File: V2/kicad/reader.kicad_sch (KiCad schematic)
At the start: 88 parts, among them SW1 SW_Rezistance, SW2 SW_src, U1 STM32H523CET6, U2 MAX98357AETE+T, U3 MLD-TF PUSH-H18, U4 TCAN1057AVDRQ1, U5 ESD2CAN24-ES, U6 RJ-064-1, U7 MCP16301Hx-xCH, Y1 16MHz

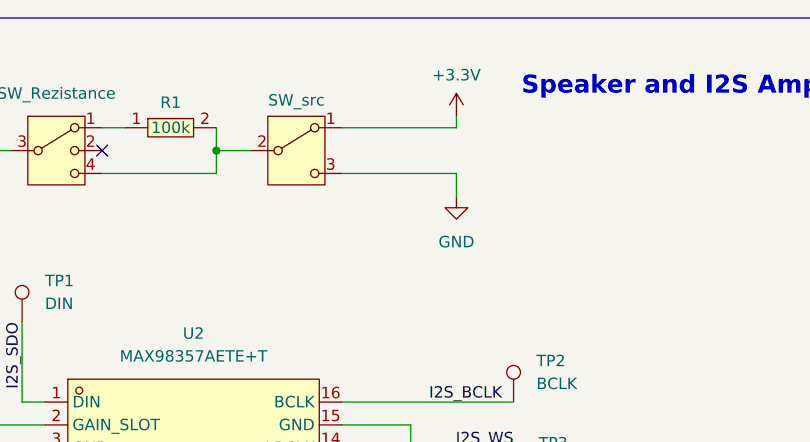
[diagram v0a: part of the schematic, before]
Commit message: changed signage in gain slot table
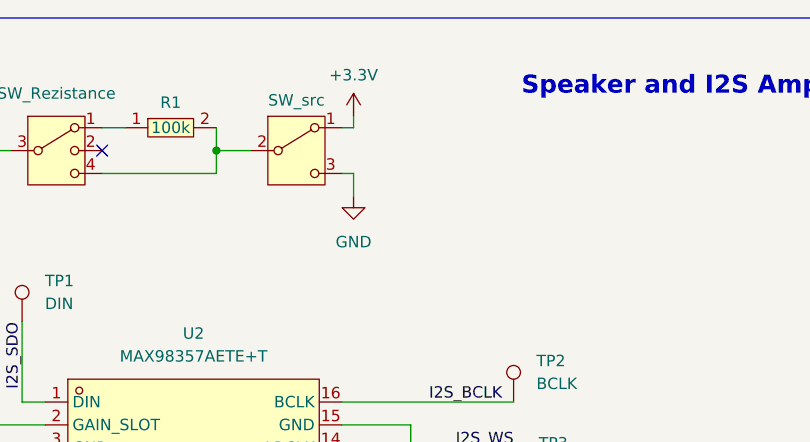
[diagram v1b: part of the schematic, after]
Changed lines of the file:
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@@
 	(wire
 		(pts
-			(xy 354.33 35.56) (xy 354.33 33.02)
+			(xy 342.9 35.56) (xy 342.9 33.02)
 		)
 		(stroke
@@
 	(wire
 		(pts
-			(xy 341.63 27.94) (xy 354.33 27.94)
+			(xy 341.63 27.94) (xy 342.9 27.94)
 		)
 		(stroke
@@
 	(wire
 		(pts
-			(xy 354.33 26.67) (xy 354.33 27.94)
+			(xy 342.9 26.67) (xy 342.9 27.94)
 		)
 		(stroke
@@
 	(wire
 		(pts
-			(xy 354.33 33.02) (xy 341.63 33.02)
+			(xy 342.9 33.02) (xy 341.63 33.02)
 		)
 		(stroke
@@
 				)
 			)
-			(table_cell "2"
+			(table_cell "1"
 				(exclude_from_sim no)
 				(at 285.242 22.352 0)
@@
 				)
 			)
-			(table_cell "3"
+			(table_cell "1"
 				(exclude_from_sim no)
 				(at 290.068 24.892 0)
@@
 				)
 			)
-			(table_cell "1"
+			(table_cell "2"
 				(exclude_from_sim no)
 				(at 285.242 27.432 0)
@@
 				)
 			)
-			(table_cell "2"
+			(table_cell "1"
 				(exclude_from_sim no)
 				(at 285.242 32.512 0)
@@
 				)
 			)
-			(table_cell "1"
+			(table_cell "3"
 				(exclude_from_sim no)
 				(at 290.068 32.512 0)
@@
 	(symbol
 		(lib_id "power:+3.3V")
-		(at 354.33 26.67 0)
+		(at 342.9 26.67 0)
 		(unit 1)
 		(body_style 1)
@@
 		(dnp no)
 		(property "Reference" "#PWR01"
-			(at 354.33 30.48 0)
+			(at 342.9 30.48 0)
 			(hide yes)
 			(show_name no)
@@
 		)
 		(property "Value" "+3.3V"
-			(at 354.33 22.098 0)
+			(at 342.9 22.098 0)
 			(show_name no)
 			(do_not_autoplace no)
@@
 		)
 		(property "Footprint" ""
-			(at 354.33 26.67 0)
+			(at 342.9 26.67 0)
 			(hide yes)
 			(show_name no)
@@
 		)
 		(property "Datasheet" ""
-			(at 354.33 26.67 0)
+			(at 342.9 26.67 0)
 			(hide yes)
 			(show_name no)
@@
 		)
 		(property "Description" "Power symbol creates a global label with name \"+3.3V\""
-			(at 354.33 26.67 0)
+			(at 342.9 26.67 0)
 			(hide yes)
 			(show_name no)
@@
 	(symbol
 		(lib_id "power:GND")
-		(at 354.33 35.56 0)
+		(at 342.9 35.56 0)
 		(unit 1)
 		(body_style 1)
@@
 		(fields_autoplaced yes)
 		(property "Reference" "#PWR02"
-			(at 354.33 41.91 0)
+			(at 342.9 41.91 0)
 			(hide yes)
 			(show_name no)
@@
 		)
 		(property "Value" "GND"
-			(at 354.33 40.64 0)
+			(at 342.9 40.64 0)
 			(show_name no)
 			(do_not_autoplace no)
@@
 		)
 		(property "Footprint" ""
-			(at 354.33 35.56 0)
+			(at 342.9 35.56 0)
 			(hide yes)
 			(show_name no)
@@
 		)
 		(property "Datasheet" ""
-			(at 354.33 35.56 0)
+			(at 342.9 35.56 0)
 			(hide yes)
 			(show_name no)
@@
 		)
 		(property "Description" "Power symbol creates a global label with name \"GND\" , ground"
-			(at 354.33 35.56 0)
+			(at 342.9 35.56 0)
 			(hide yes)
 			(show_name no)
@@
 			)
 		)
-		(property "Datasheet" "https://jlcpcb.com/api/file/downloadByFileSystemAccessId/8590908716709863424"
+		(property "Datasheet" "https://www.lcsc.com/datasheet/C6465979.pdf?spm=wm.sxq.inf.ggs&lcsc_vid=FVRbUlZVElUKAldUT1FbAVZWElcMUlFXR1FXBgVQElUxVlNeRlBeXl1SQlVfVzsOAxUeFF5JWBYZEEoKFBINSQcJGk4%3D"
 			(at 24.13 261.112 0)
 			(hide yes)
@@
 			)
 		)
-		(property "Datasheet" "https://jlcpcb.com/api/file/downloadByFileSystemAccessId/8590902847586181120"
+		(property "Datasheet" "https://www.lcsc.com/datasheet/C5553822.pdf"
 			(at 43.18 261.112 0)
 			(hide yes)

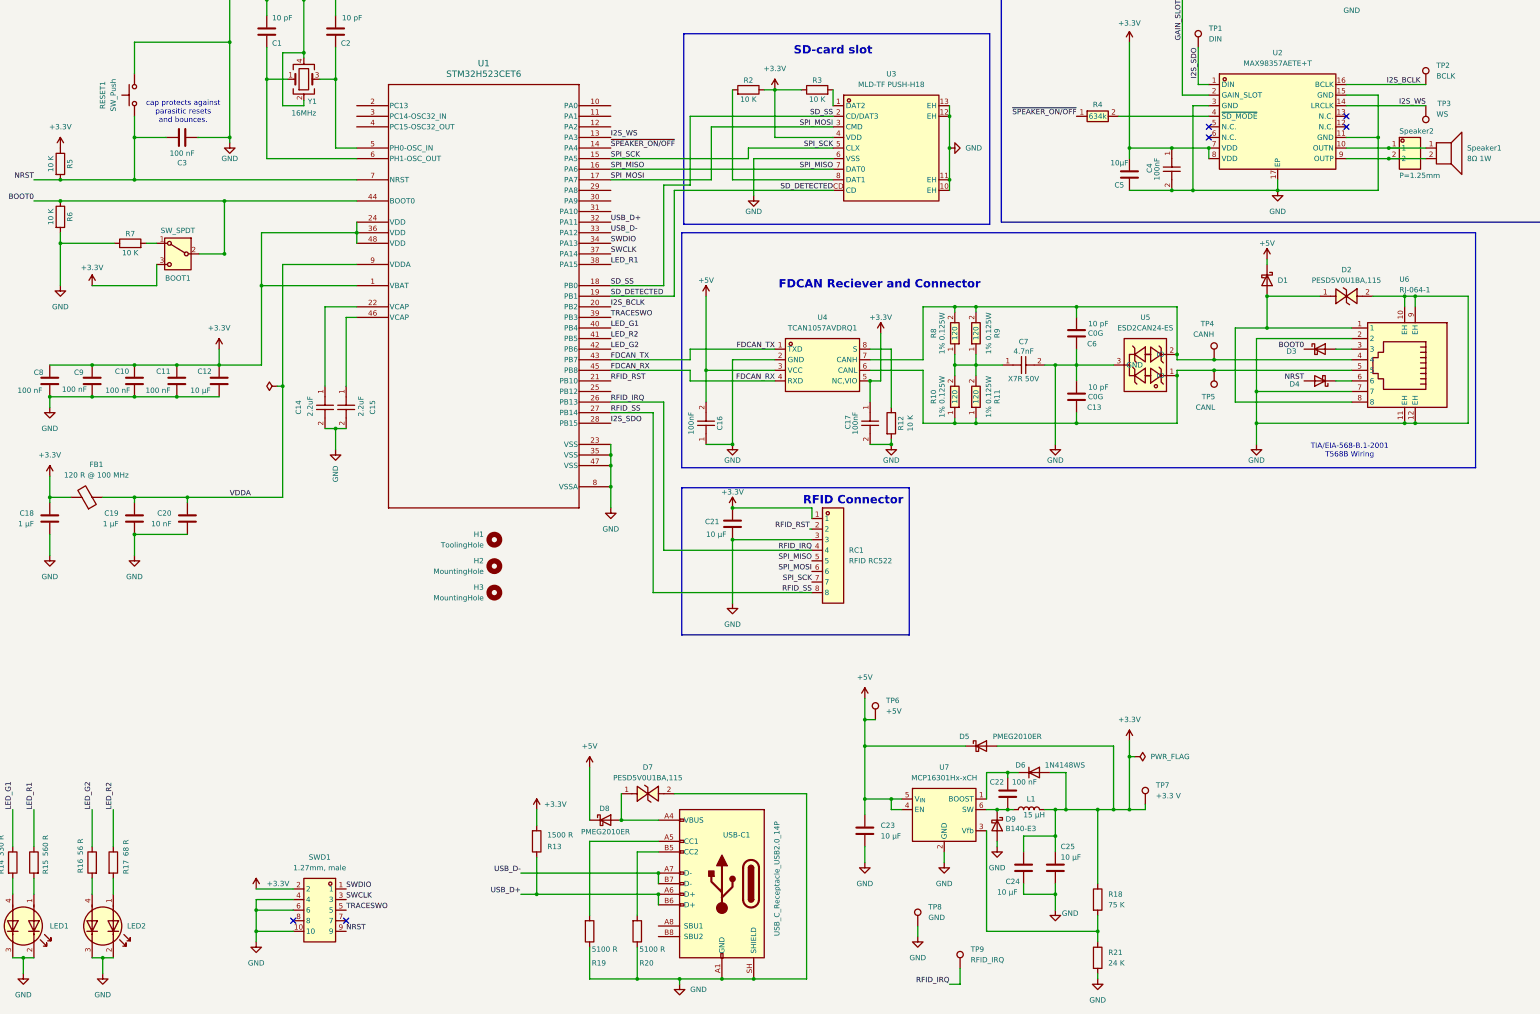
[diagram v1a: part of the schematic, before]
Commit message: changed 20mA led to 2mA led so both are same. changed orientation of card logo on back of board
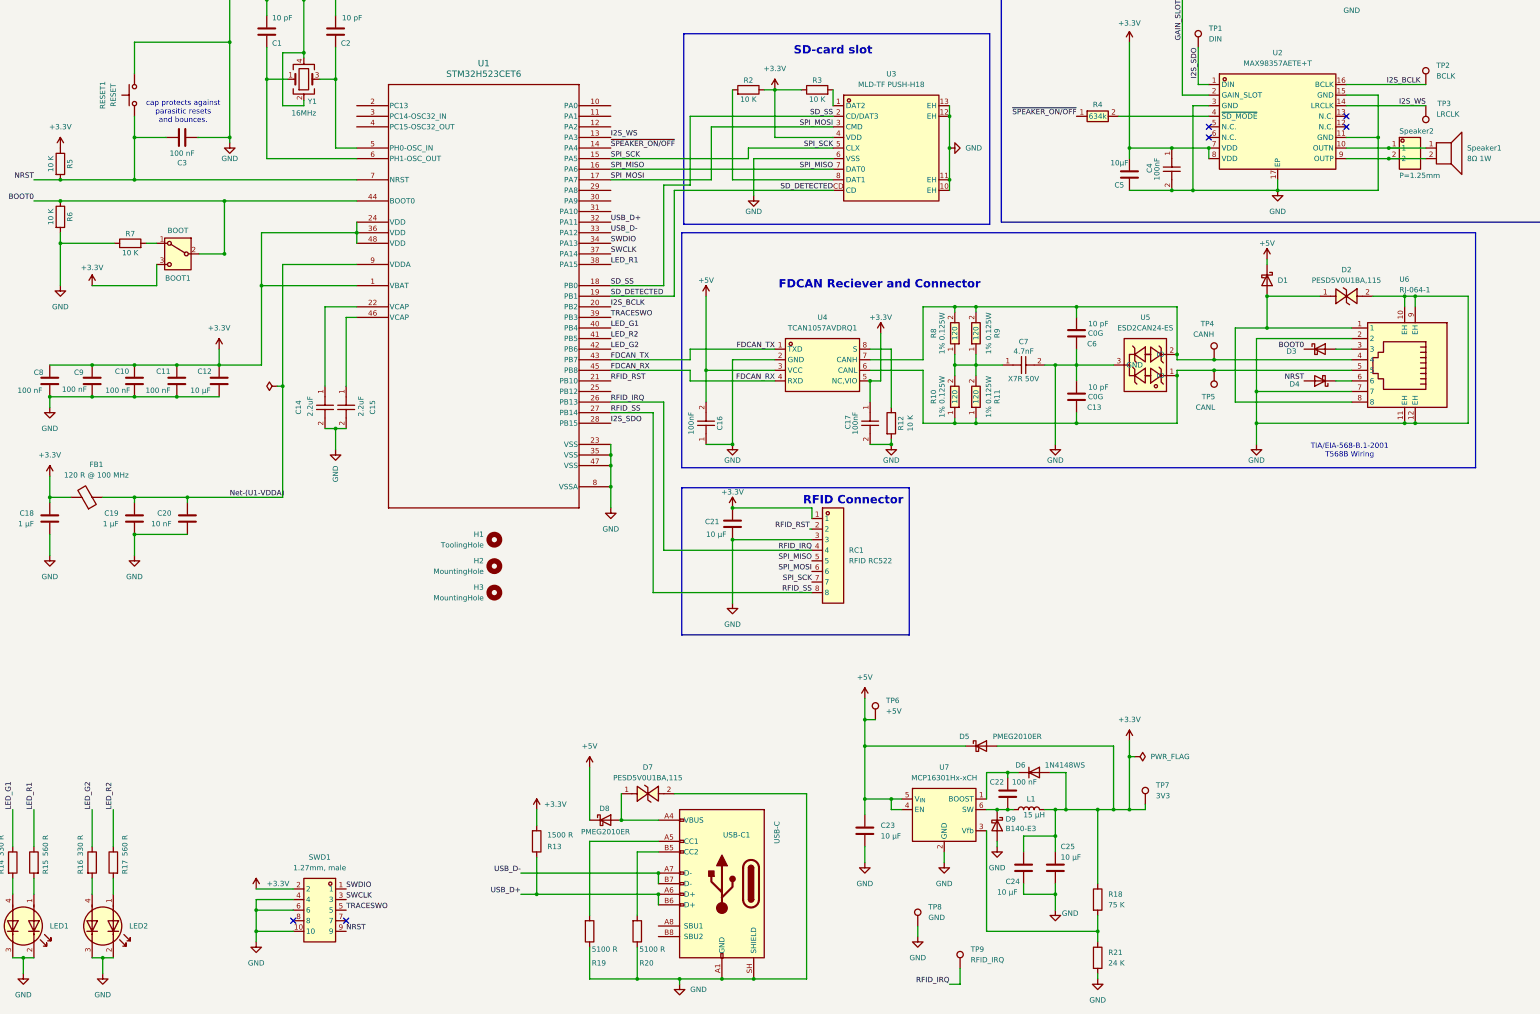
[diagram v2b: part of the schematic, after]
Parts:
- BOOT1: value SW_SPDT -> BOOT
- LED2: value APHBM2012SURKCGKC -> APHBM2012LSURKZGKC; JLCPCB https://jlcpcb.com/partdetail/Kingbright-APHBM2012SURKCGKC/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 -> https://jlcpcb.com/partdetail/Kingbright-APHBM2012LSURKZGKC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; LCSC C5553822 -> C6465979; Note 20mA, Red, Emerald, 120°, SMD-4P, 2 x 1.3 mm -> 2mA Red, Emerald, 120°, SMD-4P, 2 x 1.3 mm
- R16: value 56 R -> 330 R; JLCPCB https://jlcpcb.com/partdetail/25870-0402WGF560JTCE/C25127 -> https://jlcpcb.com/partdetail/25847-0402WGF3300TCE/C25104; LCSC C25127 -> C25104
- R17: value 68 R -> 560 R; JLCPCB https://jlcpcb.com/partdetail/Yageo-RC0402FR0768RL/C163455 -> https://jlcpcb.com/partdetail/C25126; LCSC C163455 -> C25126
- RESET1: value SW_Push -> RESET
- TP3: value WS -> LRCLK
- TP7: value +3.3 V -> 3V3
- USB-C1: value USB_C_Receptacle_USB2.0_14P -> USB-C
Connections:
- net VDDA renamed Net-(U1-VDDA)

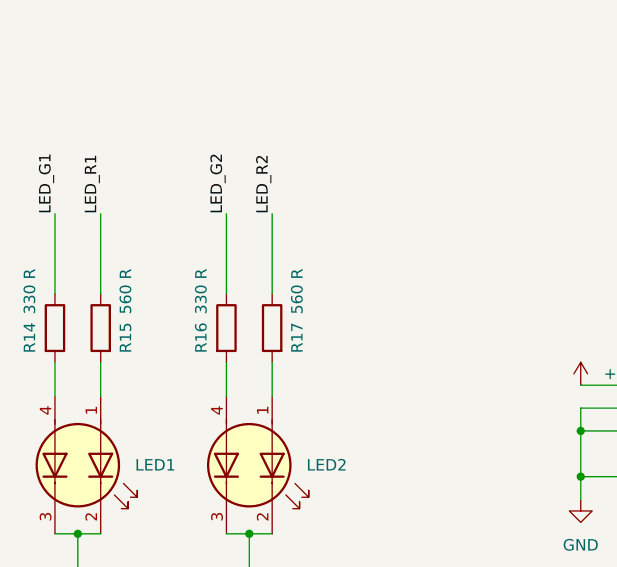
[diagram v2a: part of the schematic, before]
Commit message: changed led red color resistor from 560 to 787
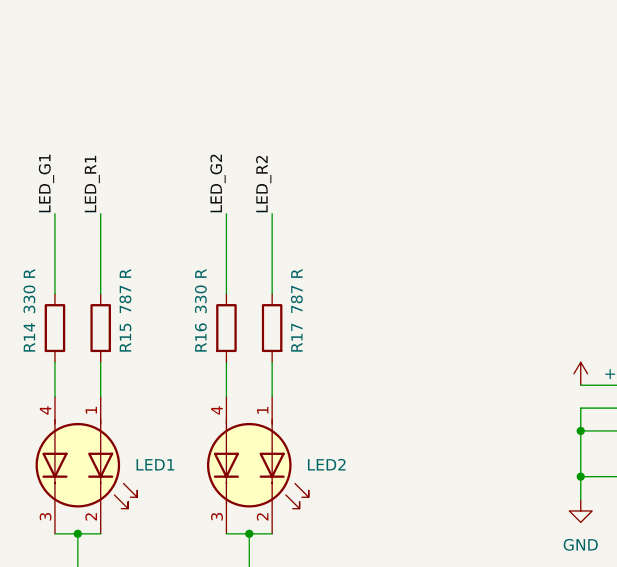
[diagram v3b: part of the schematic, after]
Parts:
- R15, R17: value 560 R -> 787 R; JLCPCB https://jlcpcb.com/partdetail/C25126 -> https://www.lcsc.com/product-detail/C270582.html; LCSC C25126 -> C270582
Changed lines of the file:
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@@
 			)
 		)
-		(property "Value" "560 R"
+		(property "Value" "787 R"
 			(at 29.464 243.586 90)
 			(show_name no)
@@
 			)
 		)
-		(property "Datasheet" "https://jlc-prod-smt.oss-eu-central-1.aliyuncs.com/smtDataManualFile/8586178278474862592-C25126.pdf?response-content-disposition=attachment%3B%20filename%3DC25126.pdf%3B%20filename%2A%3DUTF-8%27%27C25126.pdf&x-oss-date=20260603T141942Z&x-oss-expires=1800&x-oss-security-token=CAISgAN1q6Ft5B2yfSjIr5rYAPaHqJFCjrvadU%2FFs1YWQtlZrr3lsTz2IHhMdHJsAOodtv0%2FmmhT6PkclqRLcbhpcmfjV%2BZHzLB8qeAa7RNB4J7b16cNrbH4M4H6aXeirtuwDsz9SNTCALjPD3nPii50x5bjaDymRCbLGJaViJlhHLN1Ow6jdmhpCctxLAlvo9NgFxm3D%2Fu2NQPwiWf9FVdhvhEG6Vly8qOi2MaRmFy8yFTx0b0SvJ%2BjYMrmPctoN9JnSdC5mfdzau3a1TJ84gRD0a5wkaVA1zbDs5bfISEIuUzebreLqY03dV4mOvdqIcMe8qigz88fk%2FfIioH6xyxKOexoSCnFTOiiupCcQLPyao9jLu6iayqViY7QaIOTqQohZmkAMwVOasAsI3Ngh4zF97Qt0cVNkXO9gWfLI8DtuMleWhqDHsNdntHD0eS19jklBdzSlusJRAJJUVBflCeKEaRNSAd3WGhEfM2%2BBt4QT30w5N2u00S8OSMIe8fo%2BKKWD5sagAFAjLTD0371Sd2gSdBnykA7MII9CzBs0TEnncOuMMFpZ7eWxtofkMZUw83MXKFT3yGfjS9fIlx%2Bre7vtwbXSVmucxBbZSJldeqhHVomhZC6FwsraIa5cFo%2FJ2rvy%2BYXQ1kdyLEoPt0fplni6hRiSJOL598AUZr9EPV4uuEaQBdebyAA&x-oss-signature-version=OSS4-HMAC-SHA256&x-oss-credential=STS.NYmKL3ENc9y1witWVCNVuAxNS%2F20260603%2Feu-central-1%2Foss%2Faliyun_v4_request&x-oss-signature=d1629a371fbf831c62f9f7f4032d37edb65e47d37709e76674d141769ad7b5bf"
+		(property "Datasheet" "https://www.lcsc.com/datasheet/C270582.pdf?spm=wm.sxq.inf.ggs___wm.fly.bg.0.xh&lcsc_vid=FVRbUlZVElUKAldUT1FbAVZWElcMUlFXR1FXBgVQElUxVlNeRlNeUVRXQFhZVTsOAxUeFF5JWBYZEEoKFBINSQcJGk4dAgUUFAk%3D"
 			(at 26.67 245.11 0)
 			(hide yes)
@@
 			)
 		)
-		(property "JLCPCB" "https://jlcpcb.com/partdetail/C25126"
+		(property "JLCPCB" "https://www.lcsc.com/product-detail/C270582.html"
 			(at 26.67 245.11 0)
 			(hide yes)
@@
 			)
 		)
-		(property "LCSC" "C25126"
+		(property "LCSC" "C270582"
 			(at 26.67 245.11 0)
 			(hide yes)
@@
 	)
 	(symbol
+		(lib_id "Device:R")
+		(at 45.72 245.11 0)
+		(mirror y)
+		(unit 1)
+		(body_style 1)
+		(exclude_from_sim no)
+		(in_bom yes)
+		(on_board yes)
+		(in_pos_files yes)
+		(dnp no)
+		(property "Reference" "R17"
+			(at 48.514 247.904 90)
+			(show_name no)
+			(do_not_autoplace no)
+			(effects
+				(font
+					(size 1.27 1.27)
+				)
+				(justify left)
+			)
+		)
+		(property "Value" "787 R"
+			(at 48.514 243.586 90)
+			(show_name no)
+			(do_not_autoplace no)
+			(effects
+				(font
+					(size 1.27 1.27)
+				)
+				(justify left)
+			)
+		)
+		(property "Footprint" "Resistor_SMD:R_0402_1005Metric"
+			(at 47.498 245.11 90)
+			(hide yes)
+			(show_name no)
+			(do_not_autoplace no)
+			(effects
+				(font
+					(size 1.27 1.27)
+				)
+			)
+		)
+		(property "Datasheet" "https://www.lcsc.com/datasheet/C270582.pdf?spm=wm.sxq.inf.ggs___wm.fly.bg.0.xh&lcsc_vid=FVRbUlZVElUKAldUT1FbAVZWElcMUlFXR1FXBgVQElUxVlNeRlNeUVRXQFhZVTsOAxUeFF5JWBYZEEoKFBINSQcJGk4dAgUUFAk%3D"
+			(at 45.72 245.11 0)
+			(hide yes)
+			(show_name no)
+			(do_not_autoplace no)
+			(effects
+				(font
+					(size 1.27 1.27)
+				)
+			)
+		)
+		(property "Description" "Resistor"
+			(at 45.72 245.11 0)
+			(hide yes)
+			(show_name no)
+			(do_not_autoplace no)
+			(effects
+				(font
+					(size 1.27 1.27)
+				)
+			)
+		)
+		(property "Note" ""
+			(at 45.72 245.11 0)
+			(hide yes)
+			(show_name no)
+			(do_not_autoplace no)
+			(effects
+				(font
+					(size 1.27 1.27)
+				)
+			)
+		)
+		(property "JLCPCB" "https://www.lcsc.com/product-detail/C270582.html"
+			(at 45.72 245.11 0)
+			(hide yes)
+			(show_name no)
+			(do_not_autoplace no)
+			(effects
+				(font
+					(size 1.27 1.27)
+				)
+			)
+		)
+		(property "LCSC" "C270582"
+			(at 45.72 245.11 0)
+			(hide yes)
+			(show_name no)
+			(do_not_autoplace no)
+			(effects
+				(font
+					(size 1.27 1.27)
+				)
+			)
+		)
+		(property "Field5" ""
+			(at 45.72 245.11 0)
+			(hide yes)
+			(show_name no)
+			(do_not_autoplace no)
+			(effects
+				(font
+					(size 1.27 1.27)
+				)
+			)
+		)
+		(property "Field6" ""
+			(at 45.72 245.11 0)
+			(hide yes)
+			(show_name no)
+			(do_not_autoplace no)
+			(effects
+				(font
+					(size 1.27 1.27)
+				)
+			)
+		)
+		(property "KiLib_Generator" "SMD_2terminal_chip_molded"
+			(at 45.72 245.11 0)
+			(hide yes)
+			(show_name no)
+			(do_not_autoplace no)
+			(effects
+				(font
+					(size 1.27 1.27)
+				)
+			)
+		)
+		(pin "1"
+		)
+		(pin "2"
+		)
+		(instances
+			(project "reader"
+				(path "/6275a1a7-d424-4390-b849-2e49b1a9780b"
+					(reference "R17")
+					(unit 1)
+				)
+			)
+		)
+	)
+	(symbol
 		(lib_id "Device:C")
 		(at 40.64 129.54 0)
@@
 					(unit 1)
 				)
-			)
-		)
-	)
-	(symbol
-		(lib_id "Device:R")
-		(at 45.72 245.11 0)
-		(mirror y)
-		(unit 1)
-		(body_style 1)
-		(exclude_from_sim no)
-		(in_bom yes)
-		(on_board yes)
-		(in_pos_files yes)
-		(dnp no)
-		(property "Reference" "R17"
-			(at 48.514 247.904 90)
-			(show_name no)
-			(do_not_autoplace no)
-			(effects
-				(font
-					(size 1.27 1.27)
-				)
-				(justify left)
-			)
-		)
-		(property "Value" "560 R"
-			(at 48.514 243.586 90)
-			(show_name no)
-			(do_not_autoplace no)
-			(effects
-				(font
-					(size 1.27 1.27)
-				)
-				(justify left)
-			)
-		)
-		(property "Footprint" "Resistor_SMD:R_0402_1005Metric"
-			(at 47.498 245.11 90)
-			(hide yes)
-			(show_name no)
-			(do_not_autoplace no)
-			(effects
-				(font
-					(size 1.27 1.27)
-				)
-			)
-		)
-		(property "Datasheet" "https://jlc-prod-smt.oss-eu-central-1.aliyuncs.com/smtDataManualFile/8586178278474862592-C25126.pdf?response-content-disposition=attachment%3B%20filename%3DC25126.pdf%3B%20filename%2A%3DUTF-8%27%27C25126.pdf&x-oss-date=20260603T141942Z&x-oss-expires=1800&x-oss-security-token=CAISgAN1q6Ft5B2yfSjIr5rYAPaHqJFCjrvadU%2FFs1YWQtlZrr3lsTz2IHhMdHJsAOodtv0%2FmmhT6PkclqRLcbhpcmfjV%2BZHzLB8qeAa7RNB4J7b16cNrbH4M4H6aXeirtuwDsz9SNTCALjPD3nPii50x5bjaDymRCbLGJaViJlhHLN1Ow6jdmhpCctxLAlvo9NgFxm3D%2Fu2NQPwiWf9FVdhvhEG6Vly8qOi2MaRmFy8yFTx0b0SvJ%2BjYMrmPctoN9JnSdC5mfdzau3a1TJ84gRD0a5wkaVA1zbDs5bfISEIuUzebreLqY03dV4mOvdqIcMe8qigz88fk%2FfIioH6xyxKOexoSCnFTOiiupCcQLPyao9jLu6iayqViY7QaIOTqQohZmkAMwVOasAsI3Ngh4zF97Qt0cVNkXO9gWfLI8DtuMleWhqDHsNdntHD0eS19jklBdzSlusJRAJJUVBflCeKEaRNSAd3WGhEfM2%2BBt4QT30w5N2u00S8OSMIe8fo%2BKKWD5sagAFAjLTD0371Sd2gSdBnykA7MII9CzBs0TEnncOuMMFpZ7eWxtofkMZUw83MXKFT3yGfjS9fIlx%2Bre7vtwbXSVmucxBbZSJldeqhHVomhZC6FwsraIa5cFo%2FJ2rvy%2BYXQ1kdyLEoPt0fplni6hRiSJOL598AUZr9EPV4uuEaQBdebyAA&x-oss-signature-version=OSS4-HMAC-SHA256&x-oss-credential=STS.NYmKL3ENc9y1witWVCNVuAxNS%2F20260603%2Feu-central-1%2Foss%2Faliyun_v4_request&x-oss-signature=d1629a371fbf831c62f9f7f4032d37edb65e47d37709e76674d141769ad7b5bf"
-			(at 45.72 245.11 0)
-			(hide yes)
-			(show_name no)
-			(do_not_autoplace no)
-			(effects
-				(font
-					(size 1.27 1.27)
-				)
-			)
-		)
-		(property "Description" "Resistor"
-			(at 45.72 245.11 0)
-			(hide yes)
-			(show_name no)
-			(do_not_autoplace no)
-			(effects
-				(font
-					(size 1.27 1.27)
-				)
-			)
-		)
-		(property "Note" ""
-			(at 45.72 245.11 0)
-			(hide yes)
-			(show_name no)
-			(do_not_autoplace no)
-			(effects
-				(font
-					(size 1.27 1.27)
-				)
-			)
-		)
-		(property "JLCPCB" "https://jlcpcb.com/partdetail/C25126"
-			(at 45.72 245.11 0)
-			(hide yes)
-			(show_name no)
-			(do_not_autoplace no)
-			(effects
-				(font
-					(size 1.27 1.27)
-				)
-			)
-		)
-		(property "LCSC" "C25126"
-			(at 45.72 245.11 0)
-			(hide yes)
-			(show_name no)
-			(do_not_autoplace no)
-			(effects
-				(font
-					(size 1.27 1.27)
-				)
-			)
-		)
-		(property "Field5" ""
-			(at 45.72 245.11 0)
-			(hide yes)
-			(show_name no)
-			(do_not_autoplace no)
-			(effects
-				(font
-					(size 1.27 1.27)
-				)
-			)
-		)
-		(property "Field6" ""
-			(at 45.72 245.11 0)
-			(hide yes)
-			(show_name no)
-			(do_not_autoplace no)
-			(effects
-				(font
-					(size 1.27 1.27)
-				)
-			)
-		)
-		(property "KiLib_Generator" "SMD_2terminal_chip_molded"
-			(at 45.72 245.11 0)
-			(hide yes)
-			(show_name no)
-			(do_not_autoplace no)
-			(effects
-				(font
-					(size 1.27 1.27)
-				)
-			)
-		)
-		(pin "1"
-		)
-		(pin "2"
-		)
-		(instances
-			(project "reader"
-				(path "/6275a1a7-d424-4390-b849-2e49b1a9780b"
-					(reference "R17")
-					(unit 1)
-				)
